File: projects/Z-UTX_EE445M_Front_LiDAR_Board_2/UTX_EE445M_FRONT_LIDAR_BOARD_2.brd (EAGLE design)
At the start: 100.5 x 51.7 mm, 5 parts, among them IC1 EK-TM4C123GXLP

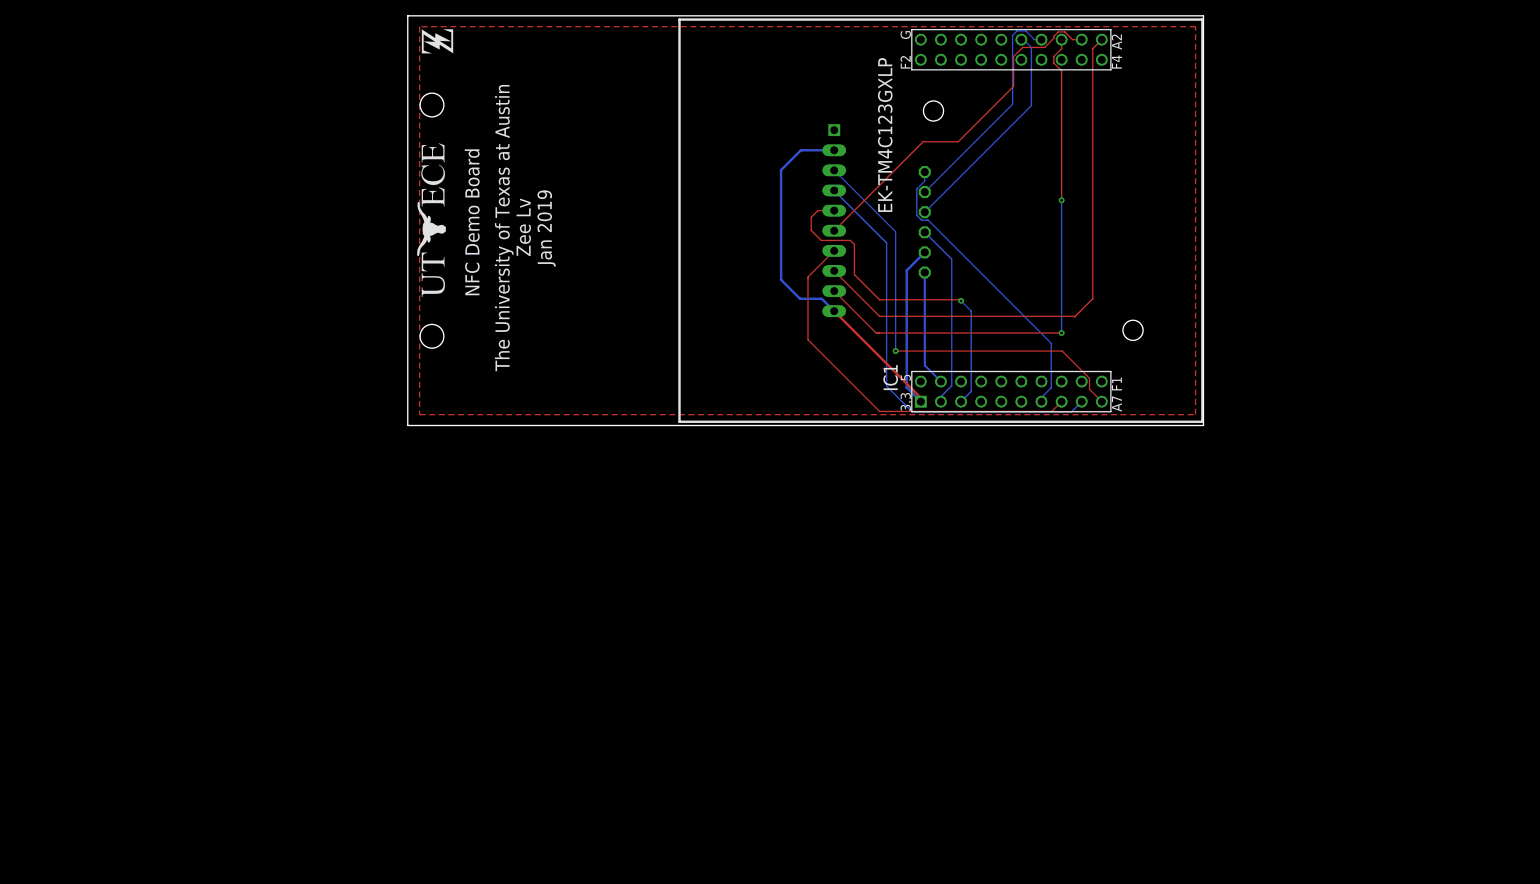
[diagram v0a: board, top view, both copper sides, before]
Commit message: add 2 new designs of UTexas EE445M front LiDAR board
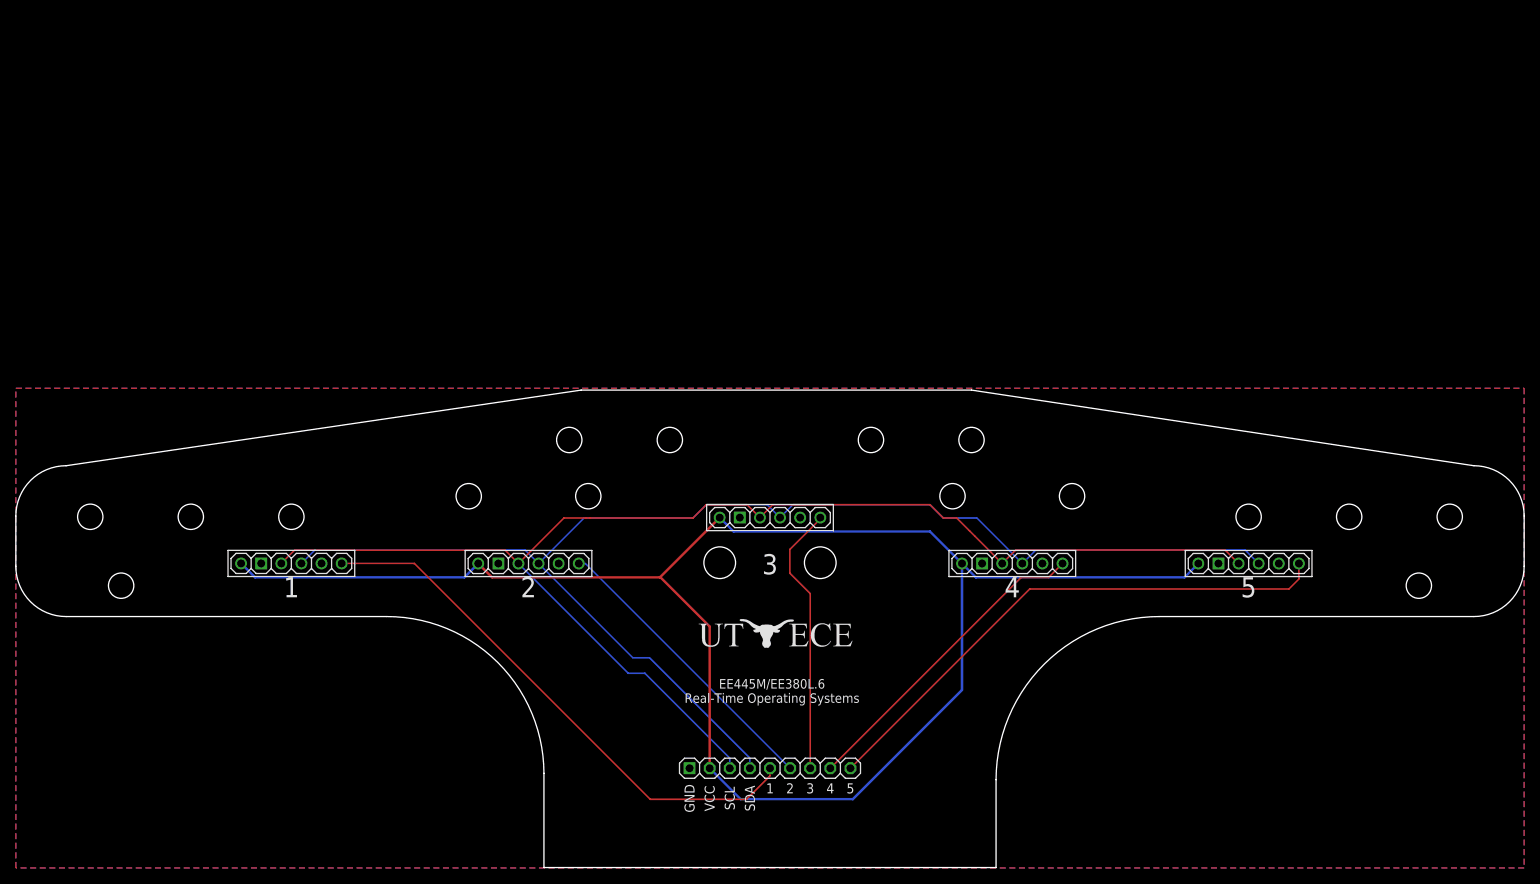
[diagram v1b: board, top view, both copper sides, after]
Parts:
- removed DIS1: ST7735, UT_ECE:ST7735
- removed IC1: EK-TM4C123GXLP, UT_ECE:TM4C123LAUNCHPAD
- added U$4, U$5, U$6: LIDAR_VL53L0X_ATK_VERT, Z:LIDAR_VL53L0X_ATK_VERT
- added U$7: (no value), Z:LOGO_UT_ECE_20X4
- added U$8: (no value), Z:LOGO_Z_3X4
- U$1: value ELECHOUSE_PN532_SPI -> UTX_EE445M_LIDAR_FRONT_BOARD_CONNECTOR_PTH; device Z:ELECHOUSE_PN532_SPI -> Z:UTX_EE445M_LIDAR_FRONT_BOARD_CONNECTOR_PTH
- U$2: value (none) -> LIDAR_VL53L0X_ATK_VERT; device Z:LOGO_UT_ECE_20X4 -> Z:LIDAR_VL53L0X_ATK_VERT
- U$3: value (none) -> LIDAR_VL53L0X_ATK_VERT; device Z:LOGO_Z_3X4 -> Z:LIDAR_VL53L0X_ATK_VERT
- moved U$1 79.0 mm to (95.2, -21.7), flipped to the top, turned to 0 degrees
- moved U$3 65.1 mm to (64.8, 6.70), turned to 0 degrees
- moved U$2 38.6 mm to (34.8, 6.71), turned to 0 degrees
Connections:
- removed net 3V3: DIS1.10, DIS1.2, IC1.1, U$1.VCC
- removed net 5V: IC1.21
- removed net SD_CS: DIS1.5, IC1.3
- removed net SSI0_MISO: DIS1.9, IC1.13
- removed net SSI0_MOSI: DIS1.7, IC1.8
- removed net SSI0_SCK: DIS1.8, IC1.11
- removed net SSI0_SS: DIS1.6, IC1.12
- removed net SSI2_MISO: IC1.14, U$1.MISO
- removed net SSI2_MOSI: IC1.15, U$1.MOSI
- removed net SSI2_SCK: IC1.7, U$1.SCK
- removed net SSI2_SS: IC1.2, U$1.SS
- removed net ST7735_DC: DIS1.4, IC1.9
- removed net ST7735_RESET: DIS1.3, IC1.10
- new net N$1: U$3.INT
- new net N$13: U$2.INT
- new net N$2: U$6.INT
- new net N$3: U$4.INT
- new net N$5: U$5.INT
- new net SCL: U$1.SCL, U$2.SCL, U$3.SCL, U$4.SCL, U$5.SCL, U$6.SCL
- new net SDA: U$1.SDA, U$2.SDA, U$3.SDA, U$4.SDA, U$5.SDA, U$6.SDA
- new net VCC: U$1.VCC, U$2.VCC, U$3.VCC, U$4.VCC, U$5.VCC, U$6.VCC
- new net XSHUT1: U$1.XSHUT1, U$2.XSH
- new net XSHUT2: U$1.XSHUT2, U$3.XSH
- new net XSHUT3: U$1.XSHUT3, U$4.XSH
- new net XSHUT4: U$1.XSHUT4, U$5.XSH
- new net XSHUT5: U$1.XSHUT5, U$6.XSH
- net GND: now also U$2.GND, U$3.GND, U$4.GND, U$5.GND, U$6.GND; no longer DIS1.1, IC1.20, IC1.22
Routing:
- net VCC: track 0.00 -> 212.0 mm
- net SDA: track 0.00 -> 169.4 mm
- net SCL: track 0.00 -> 169.3 mm
- net SSI0_SCK: track 69.2 -> 0.00 mm
- net SSI0_MISO: track 68.8 -> 0.00 mm, vias 2 -> 0
- net XSHUT1: track 0.00 -> 68.6 mm
- net XSHUT5: track 0.00 -> 68.5 mm
- net 3V3: track 66.5 -> 0.00 mm
- net ST7735_RESET: track 55.5 -> 0.00 mm, vias 1 -> 0
- net ST7735_DC: track 54.0 -> 0.00 mm
- net SSI0_MOSI: track 48.9 -> 0.00 mm
- net SSI0_SS: track 44.4 -> 0.00 mm
- net SD_CS: track 43.5 -> 0.00 mm, vias 1 -> 0
- net XSHUT4: track 0.00 -> 40.0 mm
- net SSI2_SCK: track 37.4 -> 0.00 mm
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- added copper zone on layer 16, net GND
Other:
- board size 100.5 x 51.7 mm -> 190.5 x 60.3 mm
- board text added: "1"
- board text added: "2"
- board text added: "3"
- board text added: "4"
- board text added: "5"
- board text added: "EE445M/EE380L.6 Real-Time Operating Systems"
- board text added: "University of Texas at Austin Zee Lv, Sijin Woo March 2019"
- board text removed: "NFC Demo Board"
- board text removed: "The University of Texas at Austin Zee Lv Jan 2019"
